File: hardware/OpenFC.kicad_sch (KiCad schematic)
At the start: 0 parts

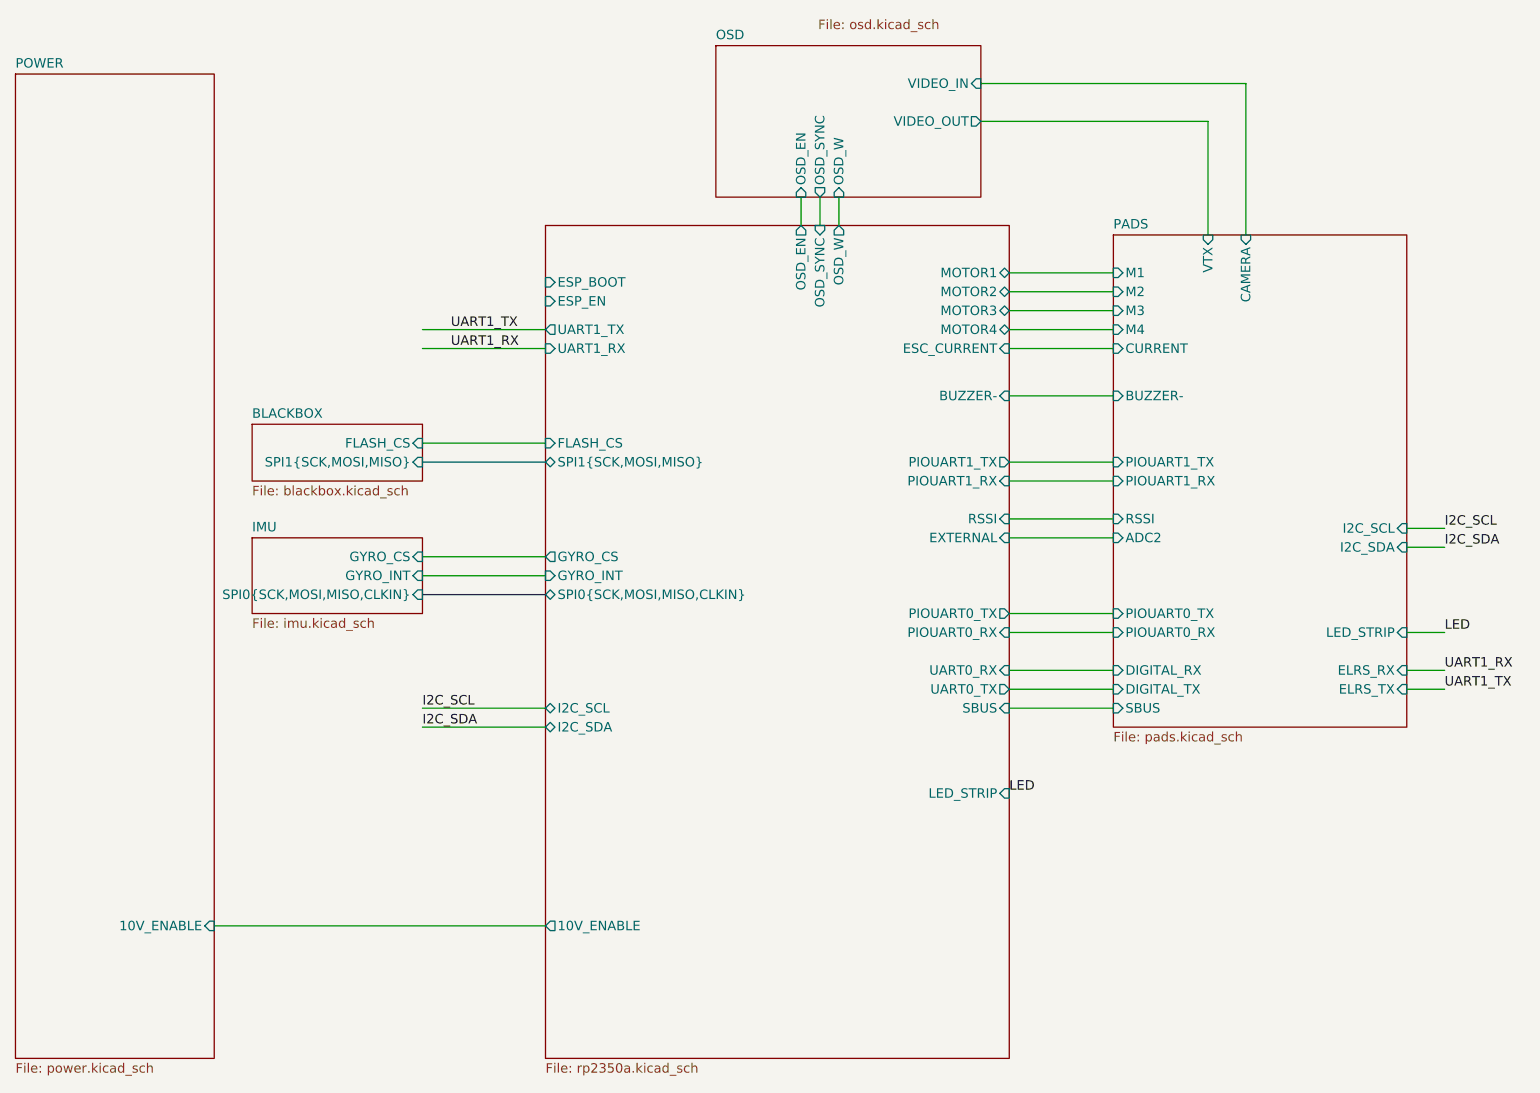
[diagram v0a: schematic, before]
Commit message: many tiny improvements
- I/O correctness
- SPI0/SPI1/I2C0 bus corrections
- decoupling of DVDD
- ADC_AVDD as per RPi documents
- removal of SBUS
- connect ESC serial
- remove RUN RC-circuit as per RPi documentation
- some more cleanup for readability
- gyro CLKIN decision
- I2C 4.7k pullup
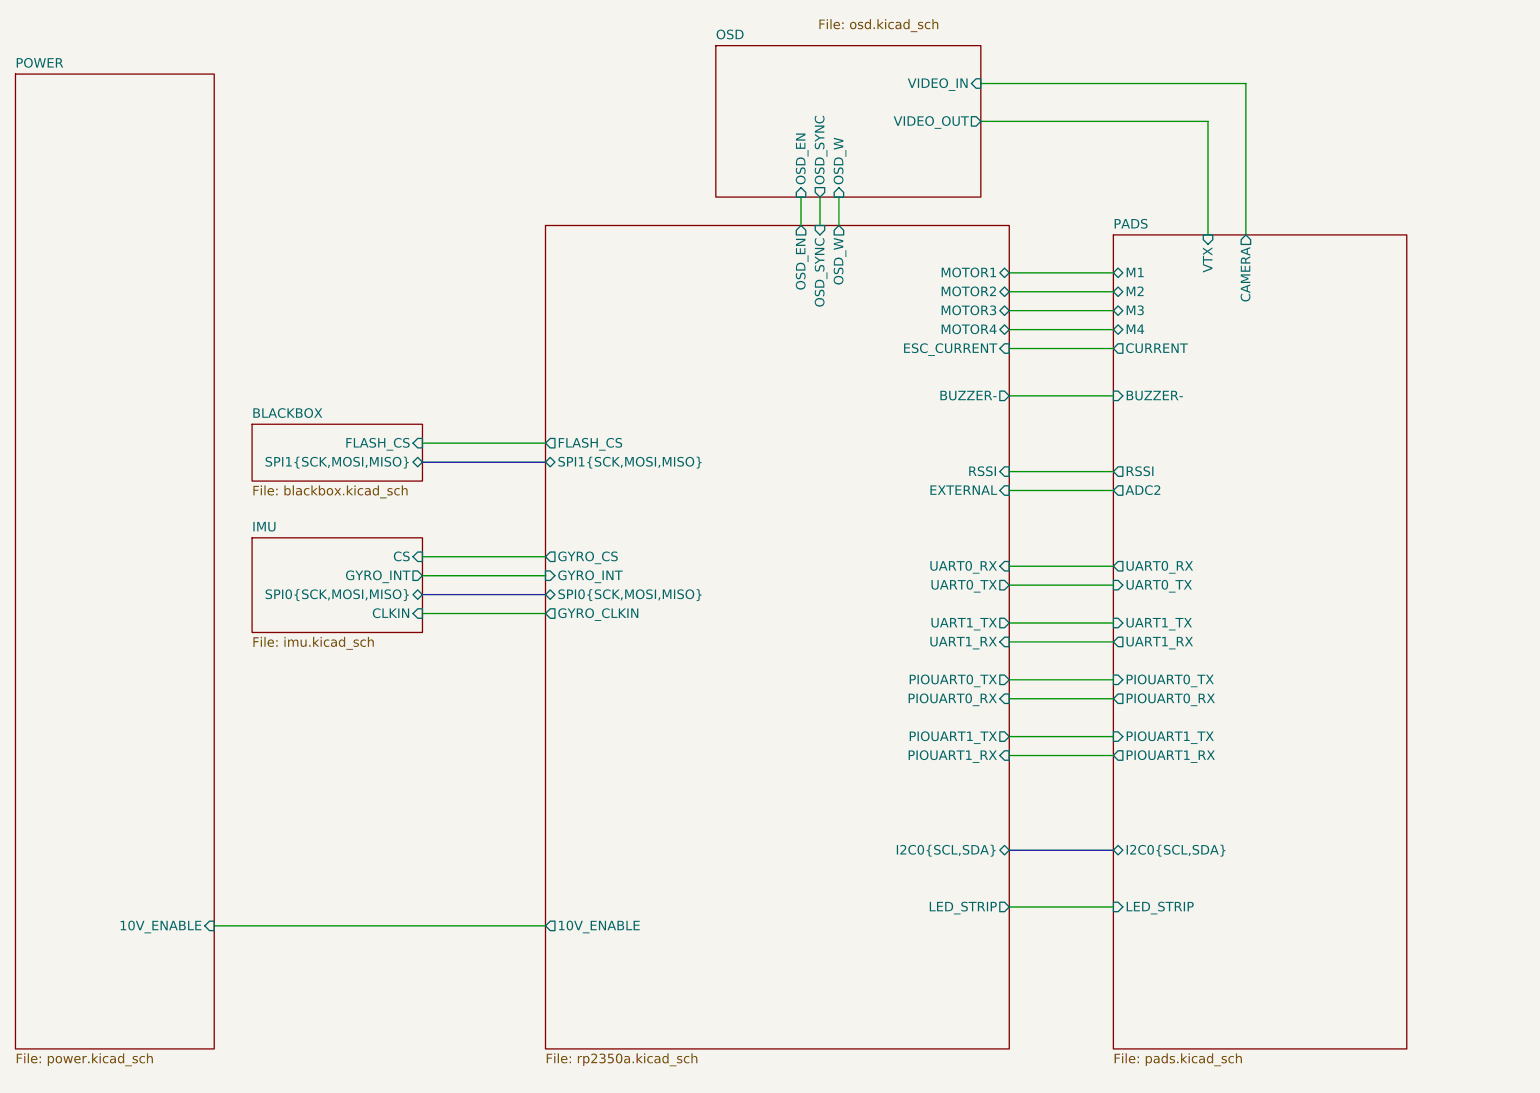
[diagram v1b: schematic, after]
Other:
- sheet IMU ports: added CLKIN, CS, SPI0{SCK,MOSI,MISO}; removed GYRO_CS, SPI0{SCK,MOSI,MISO,CLKIN}
- sheet PADS ports: added I2C0{SCL,SDA}, UART0_RX, UART0_TX, UART1_RX, UART1_TX; removed DIGITAL_RX, DIGITAL_TX, ELRS_RX, ELRS_TX, I2C_SCL, I2C_SDA, SBUS
- sheet RP2350A ports: added GYRO_CLKIN, I2C0{SCL,SDA}, SPI0{SCK,MOSI,MISO}; removed ESP_BOOT, ESP_EN, I2C_SCL, I2C_SDA, SBUS, SPI0{SCK,MOSI,MISO,CLKIN}

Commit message: RP2354A
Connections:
- no-connect marks 0 -> 5
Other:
- sheet RP2350A ports: added none; removed EXTERNAL, GYRO_CLKIN, PIOUART1_RX, PIOUART1_TX, RSSI
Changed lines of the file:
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@@
 	(generator_version "10.0")
 	(paper "A4")
+	(no_connect
+		(at 165.1 83.82)
+	)
+	(no_connect
+		(at 165.1 119.38)
+	)
+	(no_connect
+		(at 165.1 86.36)
+	)
+	(no_connect
+		(at 102.87 102.87)
+	)
+	(no_connect
+		(at 165.1 121.92)
+	)
 	(wire
 		(pts
@@
 			)
 		)
-		(pin "EXTERNAL" input
-			(at 165.1 86.36 0)
-			(effects
-				(font
-					(size 1.27 1.27)
-				)
-				(justify right)
-			)
-		)
 		(pin "FLASH_CS" output
 			(at 102.87 80.01 180)
@@
 			)
 		)
-		(pin "PIOUART1_RX" input
-			(at 165.1 121.92 0)
-			(effects
-				(font
-					(size 1.27 1.27)
-				)
-				(justify right)
-			)
-		)
-		(pin "PIOUART1_TX" output
-			(at 165.1 119.38 0)
-			(effects
-				(font
-					(size 1.27 1.27)
-				)
-				(justify right)
-			)
-		)
-		(pin "RSSI" input
-			(at 165.1 83.82 0)
-			(effects
-				(font
-					(size 1.27 1.27)
-				)
-				(justify right)
-			)
-		)
 		(pin "SPI1{SCK,MOSI,MISO}" bidirectional
 			(at 102.87 82.55 180)
@@
 			(effects
 				(font
-					(size 1.27 1.27)
-				)
-				(justify left)
-			)
-		)
-		(pin "GYRO_CLKIN" output
-			(at 102.87 102.87 180)
-			(effects
-				(font
